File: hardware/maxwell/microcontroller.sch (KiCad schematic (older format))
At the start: 16 parts

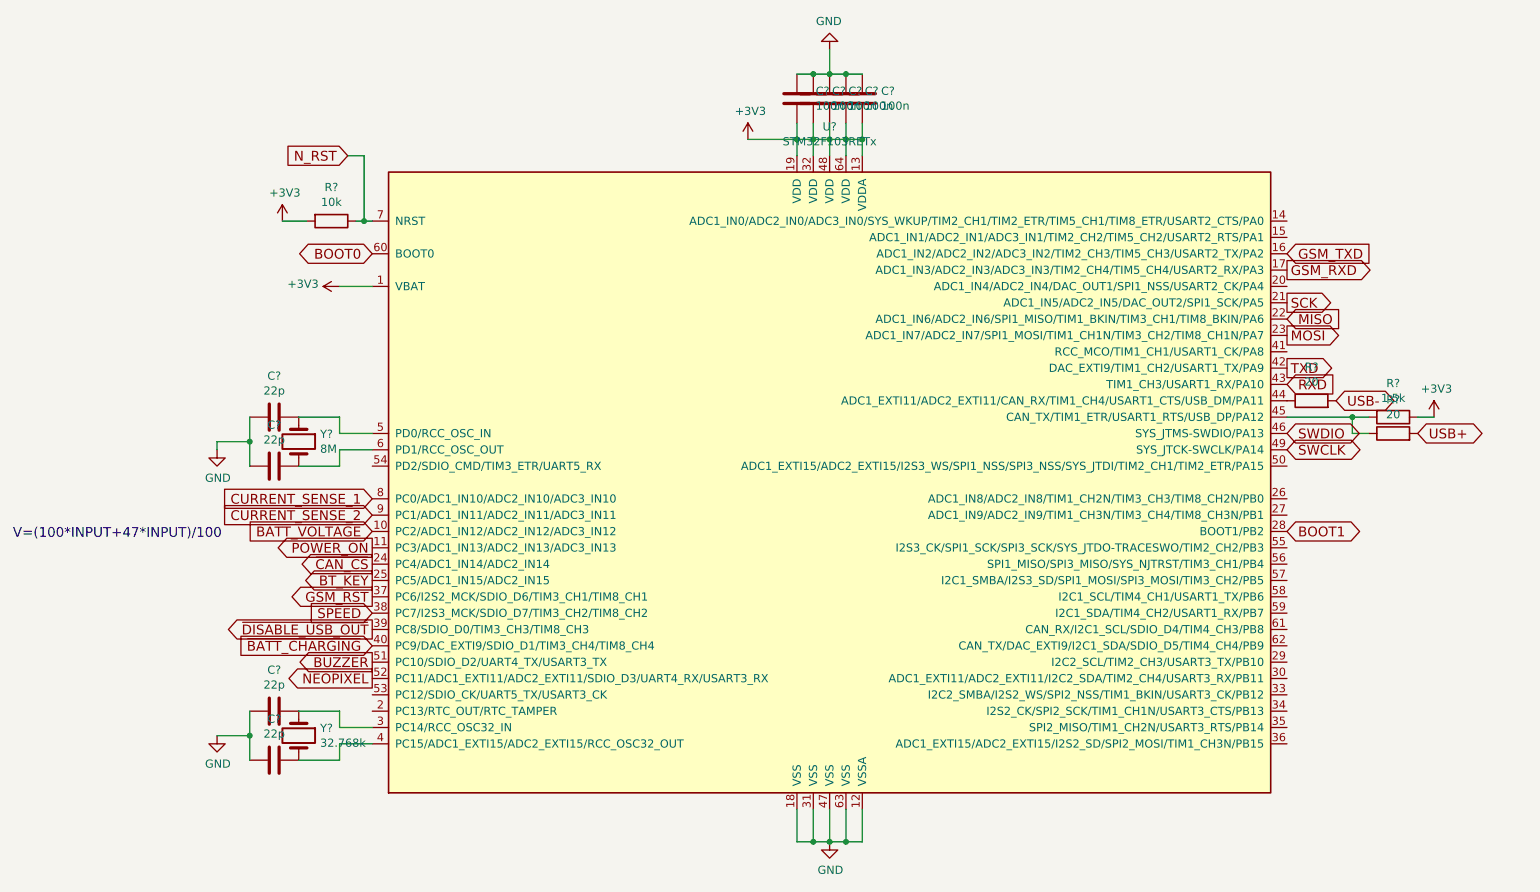
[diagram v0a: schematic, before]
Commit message: Adding finalized PCB layout.
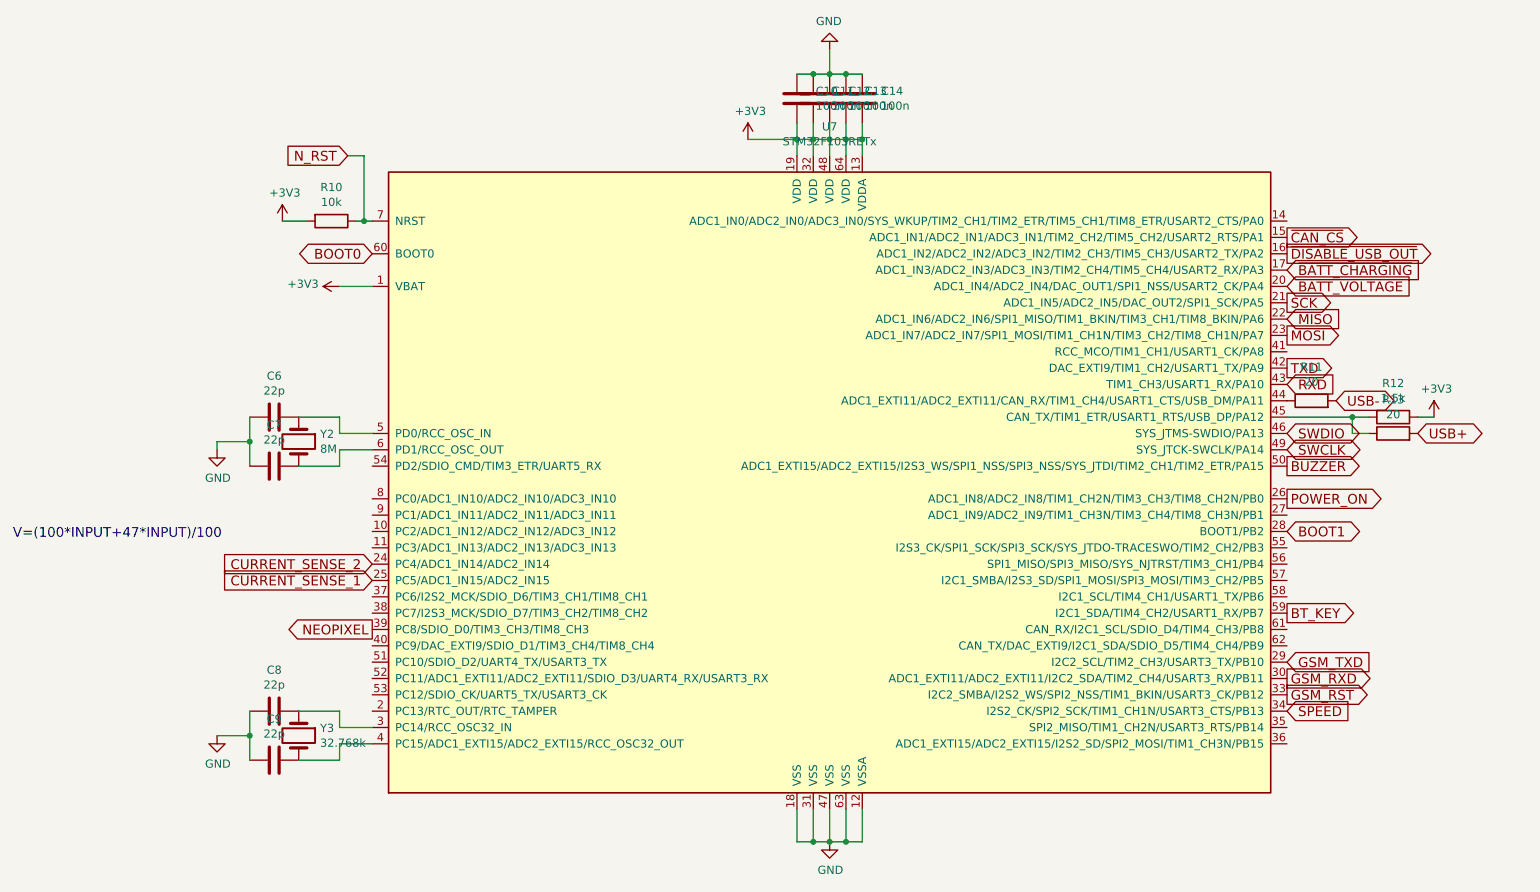
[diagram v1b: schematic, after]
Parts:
- C10, C11, C12, C13, C14, C6, C7, C8, C9: renamed from C?; footprint (none) -> coddingtonbear/coddingtonbear.pretty:0805_Milling
- R10, R11, R12, R13: renamed from R?; footprint (none) -> coddingtonbear/coddingtonbear.pretty:0805_Milling
- U7: renamed from U?; footprint LQFP64 -> kicad-castellated-breakouts:QFP64-1.27MM-CASTELLATED
- Y2: renamed from Y?; footprint (none) -> SchrodingersGat/Components.pretty:crystal_hc-49s
- Y3: renamed from Y?; footprint (none) -> f4grx/f4libs_th.pretty:XTAL32K
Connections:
- net BATT_VOLTAGE: now also U7.20 (ADC1_IN4/ADC2_IN4/DAC_OUT1/SPI1_NSS/USART2_CK/PA4); no longer U7.10 (PC2/ADC1_IN12/ADC2_IN12/ADC3_IN12)
- net BT_KEY: now also U7.59 (I2C1_SDA/TIM4_CH2/USART1_RX/PB7); no longer U7.25 (PC5/ADC1_IN15/ADC2_IN15)
- net BUZZER: now also U7.50 (ADC1_EXTI15/ADC2_EXTI15/I2S3_WS/SPI1_NSS/SPI3_NSS/SYS_JTDI/TIM2_CH1/TIM2_ETR/PA15); no longer U7.51 (PC10/SDIO_D2/UART4_TX/USART3_TX)
- net CURRENT_SENSE_1: now also U7.25 (PC5/ADC1_IN15/ADC2_IN15); no longer U7.8 (PC0/ADC1_IN10/ADC2_IN10/ADC3_IN10)
- net CURRENT_SENSE_2: now also U7.24 (PC4/ADC1_IN14/ADC2_IN14); no longer U7.9 (PC1/ADC1_IN11/ADC2_IN11/ADC3_IN11)
- net GSM_RST: now also U7.33 (I2C2_SMBA/I2S2_WS/SPI2_NSS/TIM1_BKIN/USART3_CK/PB12); no longer U7.37 (PC6/I2S2_MCK/SDIO_D6/TIM3_CH1/TIM8_CH1)
- net GSM_RXD: now also U7.30 (ADC1_EXTI11/ADC2_EXTI11/I2C2_SDA/TIM2_CH4/USART3_RX/PB11); no longer U7.17 (ADC1_IN3/ADC2_IN3/ADC3_IN3/TIM2_CH4/TIM5_CH4/USART2_RX/PA3)
- net GSM_TXD: now also U7.29 (I2C2_SCL/TIM2_CH3/USART3_TX/PB10); no longer U7.16 (ADC1_IN2/ADC2_IN2/ADC3_IN2/TIM2_CH3/TIM5_CH3/USART2_TX/PA2)
- net NEOPIXEL: now also U7.39 (PC8/SDIO_D0/TIM3_CH3/TIM8_CH3); no longer U7.52 (PC11/ADC1_EXTI11/ADC2_EXTI11/SDIO_D3/UART4_RX/USART3_RX)
- net POWER_ON: now also U7.26 (ADC1_IN8/ADC2_IN8/TIM1_CH2N/TIM3_CH3/TIM8_CH2N/PB0); no longer U7.11 (PC3/ADC1_IN13/ADC2_IN13/ADC3_IN13)
- net SPEED: now also U7.34 (I2S2_CK/SPI2_SCK/TIM1_CH1N/USART3_CTS/PB13); no longer U7.38 (PC7/I2S3_MCK/SDIO_D7/TIM3_CH2/TIM8_CH2)
- net ~BATT_CHARGING: now also U7.17 (ADC1_IN3/ADC2_IN3/ADC3_IN3/TIM2_CH4/TIM5_CH4/USART2_RX/PA3); no longer U7.40 (PC9/DAC_EXTI9/SDIO_D1/TIM3_CH4/TIM8_CH4)
- net ~CAN_CS: now also U7.15 (ADC1_IN1/ADC2_IN1/ADC3_IN1/TIM2_CH2/TIM5_CH2/USART2_RTS/PA1); no longer U7.24 (PC4/ADC1_IN14/ADC2_IN14)
- net ~DISABLE_USB_OUT: now also U7.16 (ADC1_IN2/ADC2_IN2/ADC3_IN2/TIM2_CH3/TIM5_CH3/USART2_TX/PA2); no longer U7.39 (PC8/SDIO_D0/TIM3_CH3/TIM8_CH3)
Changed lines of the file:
@@
 $EndDescr
 $Comp
-L STM32F103RETx U?
+L STM32F103RETx U7
 U 1 1 5A1FCF5C
 P 5700 3850
-F 0 "U?" H 5700 6028 50  0000 C CNN
+F 0 "U7" H 5700 6028 50  0000 C CNN
 F 1 "STM32F103RETx" H 5700 5937 50  0000 C CNN
-F 2 "LQFP64" H 8400 5725 50  0001 R TNN
+F 2 "kicad-castellated-breakouts:QFP64-1.27MM-CASTELLATED" H 8400 5725 50  0001 R TNN
 F 3 "" H 5700 3850 50  0001 C CNN
 	1    5700 3850
@@
 $EndComp
 $Comp
-L +3V3 #PWR?
+L +3V3 #PWR022
 U 1 1 5A1FCF63
 P 9400 3450
-F 0 "#PWR?" H 9400 3300 50  0001 C CNN
+F 0 "#PWR022" H 9400 3300 50  0001 C CNN
 F 1 "+3V3" H 9415 3623 50  0000 C CNN
 F 2 "" H 9400 3450 50  0001 C CNN
@@
 $EndComp
 $Comp
-L R R?
+L R R12
 U 1 1 5A1FCF69
 P 9150 3450
-F 0 "R?" V 8943 3450 50  0000 C CNN
+F 0 "R12" V 8943 3450 50  0000 C CNN
 F 1 "1.5k" V 9034 3450 50  0000 C CNN
-F 2 "" V 9080 3450 50  0001 C CNN
+F 2 "coddingtonbear/coddingtonbear.pretty:0805_Milling" V 9080 3450 50  0001 C CNN
 F 3 "" H 9150 3450 50  0001 C CNN
 	1    9150 3450
@@
 USB-
 $Comp
-L R R?
+L R R13
 U 1 1 5A1FCF77
 P 9150 3550
-F 0 "R?" V 9357 3550 50  0000 C CNN
+F 0 "R13" V 9357 3550 50  0000 C CNN
 F 1 "20" V 9266 3550 50  0000 C CNN
-F 2 "" V 9080 3550 50  0001 C CNN
+F 2 "coddingtonbear/coddingtonbear.pretty:0805_Milling" V 9080 3550 50  0001 C CNN
 F 3 "" H 9150 3550 50  0001 C CNN
 	1    9150 3550
@@
 $EndComp
 $Comp
-L R R?
+L R R11
 U 1 1 5A1FCF7E
 P 8650 3350
-F 0 "R?" V 8857 3350 50  0000 C CNN
+F 0 "R11" V 8857 3350 50  0000 C CNN
 F 1 "20" V 8766 3350 50  0000 C CNN
-F 2 "" V 8580 3350 50  0001 C CNN
+F 2 "coddingtonbear/coddingtonbear.pretty:0805_Milling" V 8580 3350 50  0001 C CNN
 F 3 "" H 8650 3350 50  0001 C CNN
 	1    8650 3350
@@
 $EndComp
 $Comp
-L Crystal Y?
+L Crystal Y2
 U 1 1 5A1FCF85
 P 2450 3600
-F 0 "Y?" V 2404 3731 50  0000 L CNN
+F 0 "Y2" V 2404 3731 50  0000 L CNN
 F 1 "8M" V 2495 3731 50  0000 L CNN
-F 2 "" H 2450 3600 50  0001 C CNN
+F 2 "SchrodingersGat/Components.pretty:crystal_hc-49s" H 2450 3600 50  0001 C CNN
 F 3 "" H 2450 3600 50  0001 C CNN
 	1    2450 3600
@@
 $EndComp
 $Comp
-L C C?
+L C C6
 U 1 1 5A1FCF8C
 P 2300 3450
-F 0 "C?" V 2048 3450 50  0000 C CNN
+F 0 "C6" V 2048 3450 50  0000 C CNN
 F 1 "22p" V 2139 3450 50  0000 C CNN
-F 2 "" H 2338 3300 50  0001 C CNN
+F 2 "coddingtonbear/coddingtonbear.pretty:0805_Milling" H 2338 3300 50  0001 C CNN
 F 3 "" H 2300 3450 50  0001 C CNN
 	1    2300 3450
@@
 $EndComp
 $Comp
-L C C?
+L C C7
 U 1 1 5A1FCF93
 P 2300 3750
-F 0 "C?" V 2048 3750 50  0000 C CNN
+F 0 "C7" V 2048 3750 50  0000 C CNN
 F 1 "22p" V 2139 3750 50  0000 C CNN
-F 2 "" H 2338 3600 50  0001 C CNN
+F 2 "coddingtonbear/coddingtonbear.pretty:0805_Milling" H 2338 3600 50  0001 C CNN
 F 3 "" H 2300 3750 50  0001 C CNN
 	1    2300 3750
@@
 $EndComp
 $Comp
-L GND #PWR?
+L GND #PWR023
 U 1 1 5A1FCF9A
 P 1950 3650
-F 0 "#PWR?" H 1950 3400 50  0001 C CNN
+F 0 "#PWR023" H 1950 3400 50  0001 C CNN
 F 1 "GND" H 1955 3477 50  0000 C CNN
 F 2 "" H 1950 3650 50  0001 C CNN
@@
 	2700 3650 2900 3650
 $Comp
-L Crystal Y?
+L Crystal Y3
 U 1 1 5A1FCFAA
 P 2450 5400
-F 0 "Y?" V 2404 5531 50  0000 L CNN
+F 0 "Y3" V 2404 5531 50  0000 L CNN
 F 1 "32.768k" V 2495 5531 50  0000 L CNN
-F 2 "" H 2450 5400 50  0001 C CNN
+F 2 "f4grx/f4libs_th.pretty:XTAL32K" H 2450 5400 50  0001 C CNN
 F 3 "" H 2450 5400 50  0001 C CNN
 	1    2450 5400
@@
 $EndComp
 $Comp
-L C C?
+L C C8
 U 1 1 5A1FCFB1
 P 2300 5250
-F 0 "C?" V 2048 5250 50  0000 C CNN
+F 0 "C8" V 2048 5250 50  0000 C CNN
 F 1 "22p" V 2139 5250 50  0000 C CNN
-F 2 "" H 2338 5100 50  0001 C CNN
+F 2 "coddingtonbear/coddingtonbear.pretty:0805_Milling" H 2338 5100 50  0001 C CNN
 F 3 "" H 2300 5250 50  0001 C CNN
 	1    2300 5250
@@
 $EndComp
 $Comp
-L C C?
+L C C9
 U 1 1 5A1FCFB8
 P 2300 5550
-F 0 "C?" V 2048 5550 50  0000 C CNN
+F 0 "C9" V 2048 5550 50  0000 C CNN
 F 1 "22p" V 2139 5550 50  0000 C CNN
-F 2 "" H 2338 5400 50  0001 C CNN
+F 2 "coddingtonbear/coddingtonbear.pretty:0805_Milling" H 2338 5400 50  0001 C CNN
 F 3 "" H 2300 5550 50  0001 C CNN
 	1    2300 5550
@@
 $EndComp
 $Comp
-L GND #PWR?
+L GND #PWR024
 U 1 1 5A1FCFBF
 P 1950 5400
-F 0 "#PWR?" H 1950 5150 50  0001 C CNN
+F 0 "#PWR024" H 1950 5150 50  0001 C CNN
 F 1 "GND" H 1955 5227 50  0000 C CNN
 F 2 "" H 1950 5400 50  0001 C CNN
@@
 Connection ~ 2150 5400
 $Comp
-L GND #PWR?
+L GND #PWR025
 U 1 1 5A1FCFCE
 P 5700 6050
-F 0 "#PWR?" H 5700 5800 50  0001 C CNN
+F 0 "#PWR025" H 5700 5800 50  0001 C CNN
 F 1 "GND" H 5705 5877 50  0000 C CNN
 F 2 "" H 5700 6050 50  0001 C CNN
@@
 BOOT0
 $Comp
-L R R?
+L R R10
 U 1 1 5A1FCFDF
 P 2650 2250
-F 0 "R?" V 2443 2250 50  0000 C CNN
+F 0 "R10" V 2443 2250 50  0000 C CNN
 F 1 "10k" V 2534 2250 50  0000 C CNN
-F 2 "" V 2580 2250 50  0001 C CNN
+F 2 "coddingtonbear/coddingtonbear.pretty:0805_Milling" V 2580 2250 50  0001 C CNN
 F 3 "" H 2650 2250 50  0001 C CNN
 	1    2650 2250
@@
 $EndComp
 $Comp
-L +3V3 #PWR?
+L +3V3 #PWR026
 U 1 1 5A1FCFE6
 P 2350 2250
-F 0 "#PWR?" H 2350 2100 50  0001 C CNN
+F 0 "#PWR026" H 2350 2100 50  0001 C CNN
 F 1 "+3V3" H 2365 2423 50  0000 C CNN
 F 2 "" H 2350 2250 50  0001 C CNN
@@
 	2500 2250 2350 2250
 $Comp
-L C C?
+L C C10
 U 1 1 5A1FCFEE
 P 5500 1500
-F 0 "C?" H 5385 1454 50  0000 R CNN
+F 0 "C10" H 5385 1454 50  0000 R CNN
 F 1 "100n" H 5385 1545 50  0000 R CNN
-F 2 "" H 5538 1350 50  0001 C CNN
+F 2 "coddingtonbear/coddingtonbear.pretty:0805_Milling" H 5538 1350 50  0001 C CNN
 F 3 "" H 5500 1500 50  0001 C CNN
 	1    5500 1500
@@
 $EndComp
 $Comp
-L C C?
+L C C11
 U 1 1 5A1FCFF5
 P 5600 1500
-F 0 "C?" H 5485 1454 50  0000 R CNN
+F 0 "C11" H 5485 1454 50  0000 R CNN
 F 1 "100n" H 5485 1545 50  0000 R CNN
-F 2 "" H 5638 1350 50  0001 C CNN
+F 2 "coddingtonbear/coddingtonbear.pretty:0805_Milling" H 5638 1350 50  0001 C CNN
 F 3 "" H 5600 1500 50  0001 C CNN
 	1    5600 1500
@@
 $EndComp
 $Comp
-L C C?
+L C C12
 U 1 1 5A1FCFFC
 P 5700 1500
-F 0 "C?" H 5585 1454 50  0000 R CNN
+F 0 "C12" H 5585 1454 50  0000 R CNN
 F 1 "100n" H 5585 1545 50  0000 R CNN
-F 2 "" H 5738 1350 50  0001 C CNN
+F 2 "coddingtonbear/coddingtonbear.pretty:0805_Milling" H 5738 1350 50  0001 C CNN
 F 3 "" H 5700 1500 50  0001 C CNN
 	1    5700 1500
@@
 $EndComp
 $Comp
-L C C?
+L C C13
 U 1 1 5A1FD003
 P 5800 1500
-F 0 "C?" H 5685 1454 50  0000 R CNN
+F 0 "C13" H 5685 1454 50  0000 R CNN
 F 1 "100n" H 5685 1545 50  0000 R CNN
-F 2 "" H 5838 1350 50  0001 C CNN
+F 2 "coddingtonbear/coddingtonbear.pretty:0805_Milling" H 5838 1350 50  0001 C CNN
 F 3 "" H 5800 1500 50  0001 C CNN
 	1    5800 1500
@@
 $EndComp
 $Comp
-L C C?
+L C C14
 U 1 1 5A1FD00A
 P 5900 1500
-F 0 "C?" H 5785 1454 50  0000 R CNN
+F 0 "C14" H 5785 1454 50  0000 R CNN
 F 1 "100n" H 5785 1545 50  0000 R CNN
-F 2 "" H 5938 1350 50  0001 C CNN
+F 2 "coddingtonbear/coddingtonbear.pretty:0805_Milling" H 5938 1350 50  0001 C CNN
 F 3 "" H 5900 1500 50  0001 C CNN
 	1    5900 1500
@@
 $EndComp
 $Comp
-L GND #PWR?
+L GND #PWR027
 U 1 1 5A1FD011
 P 5700 1200
-F 0 "#PWR?" H 5700 950 50  0001 C CNN
+F 0 "#PWR027" H 5700 950 50  0001 C CNN
 F 1 "GND" H 5705 1027 50  0000 C CNN
 F 2 "" H 5700 1200 50  0001 C CNN
@@
 $EndComp
 $Comp
-L +3V3 #PWR?
+L +3V3 #PWR028
 U 1 1 5A1FD017
 P 5200 1750
-F 0 "#PWR?" H 5200 1600 50  0001 C CNN
+F 0 "#PWR028" H 5200 1600 50  0001 C CNN
 F 1 "+3V3" H 5215 1923 50  0000 C CNN
 F 2 "" H 5200 1750 50  0001 C CNN
@@
 	5700 1200 5700 1350
 $Comp
-L +3V3 #PWR?
+L +3V3 #PWR029
 U 1 1 5A1FD02D
 P 2700 2650
-F 0 "#PWR?" H 2700 2500 50  0001 C CNN
+F 0 "#PWR029" H 2700 2500 50  0001 C CNN
 F 1 "+3V3" V 2715 2778 50  0000 L CNN
 F 2 "" H 2700 2650 50  0001 C CNN
@@
 Text GLabel 8500 3650 2    60   BiDi ~ 0
 SWCLK
-Text GLabel 2900 4650 0    60   Input ~ 0
+Text GLabel 8500 5250 2    60   Input ~ 0
 SPEED
-Text GLabel 2900 4750 0    60   Output ~ 0
+Text GLabel 8500 2450 2    60   Output ~ 0
 ~DISABLE_USB_OUT
-Text GLabel 2900 4850 0    60   Input ~ 0
+Text GLabel 8500 2550 2    60   Input ~ 0
 ~BATT_CHARGING
-Text GLabel 2900 4250 0    60   Output ~ 0
+Text GLabel 8500 3950 2    60   Output ~ 0
 POWER_ON
 Text GLabel 8500 2750 2    60   Output ~ 0
@@
 Text GLabel 8500 2950 2    60   Output ~ 0
 MOSI
-Text GLabel 2900 4350 0    60   Output ~ 0
+Text GLabel 8500 2350 2    60   Output ~ 0
 ~CAN_CS
 Text GLabel 8500 3150 2    60   Output ~ 0
@@
 Text GLabel 8500 3250 2    60   Input ~ 0
 RXD
-Text GLabel 2900 4450 0    60   Output ~ 0
+Text GLabel 8500 4650 2    60   Output ~ 0
 BT_KEY
-Text GLabel 8500 2450 2    60   Input ~ 0
+Text GLabel 8500 4950 2    60   Input ~ 0
 GSM_TXD
-Text GLabel 8500 2550 2    60   Output ~ 0
+Text GLabel 8500 5050 2    60   Output ~ 0
 GSM_RXD
-Text GLabel 2900 4550 0    60   Output ~ 0
+Text GLabel 8500 5150 2    60   Output ~ 0
 GSM_RST
-Text GLabel 2900 3950 0    60   Input ~ 0
+Text GLabel 2900 4450 0    60   Input ~ 0
 CURRENT_SENSE_1
-Text GLabel 2900 4050 0    60   Input ~ 0
+Text GLabel 2900 4350 0    60   Input ~ 0
 CURRENT_SENSE_2
-Text GLabel 2900 4150 0    60   Input ~ 0
+Text GLabel 8500 2650 2    60   Input ~ 0
 BATT_VOLTAGE
 Text Notes 700  4200 0    60   ~ 0
 V=(100*INPUT+47*INPUT)/100
-Text GLabel 2900 4950 0    60   Output ~ 0
+Text GLabel 8500 3750 2    60   Output ~ 0
 BUZZER
-Text GLabel 2900 5050 0    60   Output ~ 0
+Text GLabel 2900 4750 0    60   Output ~ 0
 NEOPIXEL
 Text GLabel 2750 1850 0    60   Input ~ 0

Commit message: Updating schematic to add reverse polarity protection, higher-current diodes for zener limiting, and a low-side n-channel mosfet for enabling/disabling devices receiving direct battery power (limiting that quiescent current as much as possible).
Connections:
- net ENABLE_BATT_POWER: now reaches U7.62 (CAN_TX/DAC_EXTI9/I2C1_SDA/SDIO_D5/TIM4_CH4/PB9)
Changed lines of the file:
@@
 	2850 1850 2850 2250
 Connection ~ 2850 2250
+Text GLabel 8500 4850 2    60   Output ~ 0
+ENABLE_BATT_POWER
 $EndSCHEMATC

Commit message: More minor changes and fixes.
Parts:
- added R26: 1k, coddingtonbear/coddingtonbear.pretty:0805_Milling, symbol R
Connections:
- net POWER_ON: now also R26.1; no longer U7.26 (ADC1_IN8/ADC2_IN8/TIM1_CH2N/TIM3_CH3/TIM8_CH2N/PB0)
- net USB_PRER-: now reaches R11.1, U7.44 (ADC1_EXTI11/ADC2_EXTI11/CAN_RX/TIM1_CH4/USART1_CTS/USB_DM/PA11)
- net USB_PRER+: now reaches R12.2, R13.1, U7.45 (CAN_TX/TIM1_ETR/USART1_RTS/USB_DP/PA12)
- net ~DISABLE_USB_OUT renamed ENABLE_USB_OUT
- new net: R26.2, U7.26 (ADC1_IN8/ADC2_IN8/TIM1_CH2N/TIM3_CH3/TIM8_CH2N/PB0)
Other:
- moved on the sheet: R11
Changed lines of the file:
@@
 	8900 3550 8900 3450
 Connection ~ 8900 3450
-Text GLabel 8800 3350 2    60   BiDi ~ 0
+Text GLabel 9550 3350 2    60   BiDi ~ 0
 USB-
 $Comp
@@
 L R R11
 U 1 1 5A1FCF7E
-P 8650 3350
-F 0 "R11" V 8857 3350 50  0000 C CNN
-F 1 "20" V 8766 3350 50  0000 C CNN
-F 2 "coddingtonbear/coddingtonbear.pretty:0805_Milling" V 8580 3350 50  0001 C CNN
-F 3 "" H 8650 3350 50  0001 C CNN
-	1    8650 3350
+P 9400 3350
+F 0 "R11" V 9607 3350 50  0000 C CNN
+F 1 "20" V 9516 3350 50  0000 C CNN
+F 2 "coddingtonbear/coddingtonbear.pretty:0805_Milling" V 9330 3350 50  0001 C CNN
+F 3 "" H 9400 3350 50  0001 C CNN
+	1    9400 3350
 	0    -1   -1   0
 $EndComp
@@
 SPEED
 Text GLabel 8500 2450 2    60   Output ~ 0
-~DISABLE_USB_OUT
+ENABLE_USB_OUT
 Text GLabel 8500 2550 2    60   Input ~ 0
 ~BATT_CHARGING
-Text GLabel 8500 3950 2    60   Output ~ 0
+Text GLabel 8800 3950 2    60   Output ~ 0
 POWER_ON
 Text GLabel 8500 2750 2    60   Output ~ 0
@@
 Text GLabel 8500 4850 2    60   Output ~ 0
 ENABLE_BATT_POWER
+$Comp
+L R R26
+U 1 1 5A260AAF
+P 8650 3950
+F 0 "R26" V 8443 3950 50  0000 C CNN
+F 1 "1k" V 8534 3950 50  0000 C CNN
+F 2 "coddingtonbear/coddingtonbear.pretty:0805_Milling" V 8580 3950 50  0001 C CNN
+F 3 "" H 8650 3950 50  0001 C CNN
+	1    8650 3950
+	0    1    1    0
+$EndComp
+Wire Wire Line
+	8500 3350 9250 3350
+Text Label 8600 3350 0    60   ~ 0
+USB_PRER-
+Text Label 8600 3450 0    60   ~ 0
+USB_PRER+
 $EndSCHEMATC

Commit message: More fixes, additions, improvements.
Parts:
- added R33: 1M, coddingtonbear/coddingtonbear.pretty:0805_Milling, symbol R
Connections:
- net CAN_INT: now reaches U7.14 (ADC1_IN0/ADC2_IN0/ADC3_IN0/SYS_WKUP/TIM2_CH1/TIM2_ETR/TIM5_CH1/TIM8_ETR/USART2_CTS/PA0)
- net DYNAMO_VOLTAGE: now reaches U7.27 (ADC1_IN9/ADC2_IN9/TIM1_CH3N/TIM3_CH4/TIM8_CH3N/PB1)
- net BATT_CHARGE_ENABLE: now reaches U7.35 (SPI2_MISO/TIM1_CH2N/USART3_RTS/PB14)
- net at C6.1, U7.5 (PD0/RCC_OSC_IN), Y2.1: now also R33.2
- net at C7.1, U7.6 (PD1/RCC_OSC_OUT), Y2.2: now also R33.1
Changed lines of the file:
@@
 	1950 3600 2150 3600
 Connection ~ 2150 3600
-Wire Wire Line
-	2450 3450 2700 3450
-Wire Wire Line
-	2700 3450 2700 3550
-Wire Wire Line
-	2700 3550 2900 3550
-Wire Wire Line
-	2450 3750 2700 3750
-Wire Wire Line
-	2700 3750 2700 3650
-Wire Wire Line
-	2700 3650 2900 3650
 $Comp
 L Crystal Y3
@@
 	1    0    0    -1
 $EndComp
-Wire Wire Line
-	2450 5250 2700 5250
-Wire Wire Line
-	2700 5250 2700 5350
-Wire Wire Line
-	2700 5350 2900 5350
-Wire Wire Line
-	2450 5550 2700 5550
-Wire Wire Line
-	2700 5550 2700 5450
-Wire Wire Line
-	2700 5450 2900 5450
 Wire Wire Line
 	2150 5250 2150 5550
@@
 Text Label 8600 3450 0    60   ~ 0
 USB_PRER+
+Text GLabel 8500 2250 2    60   Input ~ 0
+CAN_INT
+$Comp
+L R R33
+U 1 1 5A2732F7
+P 2700 3600
+F 0 "R33" V 2493 3600 50  0000 C CNN
+F 1 "1M" V 2584 3600 50  0000 C CNN
+F 2 "coddingtonbear/coddingtonbear.pretty:0805_Milling" V 2630 3600 50  0001 C CNN
+F 3 "" H 2700 3600 50  0001 C CNN
+	1    2700 3600
+	-1   0    0    1
+$EndComp
+Wire Wire Line
+	2450 5250 2800 5250
+Wire Wire Line
+	2800 5250 2800 5350
+Wire Wire Line
+	2800 5350 2900 5350
+Wire Wire Line
+	2900 5450 2800 5450
+Wire Wire Line
+	2800 5450 2800 5550
+Wire Wire Line
+	2800 5550 2450 5550
+Wire Wire Line
+	2450 3450 2800 3450
+Wire Wire Line
+	2800 3450 2800 3550
+Wire Wire Line
+	2800 3550 2900 3550
+Connection ~ 2700 3450
+Wire Wire Line
+	2450 3750 2800 3750
+Wire Wire Line
+	2800 3750 2800 3650
+Wire Wire Line
+	2800 3650 2900 3650
+Connection ~ 2700 3750
+Text GLabel 8500 4050 2    60   Input ~ 0
+DYNAMO_VOLTAGE
+Text GLabel 8500 5350 2    60   Output ~ 0
+BATT_CHARGE_ENABLE
 $EndSCHEMATC

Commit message: Fixed just...an unbelievable number of bugs.
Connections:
- net BUZZER: now also U7.58 (I2C1_SCL/TIM4_CH1/USART1_TX/PB6); no longer U7.50 (ADC1_EXTI15/ADC2_EXTI15/I2S3_WS/SPI1_NSS/SPI3_NSS/SYS_JTDI/TIM2_CH1/TIM2_ETR/PA15)
- net BATT_CHARGE_ENABLE renamed ~BATT_CHARGE_ENABLE
- net ENABLE_USB_OUT renamed ~ENABLE_USB_OUT
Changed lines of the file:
@@
 SPEED
 Text GLabel 8500 2450 2    60   Output ~ 0
-ENABLE_USB_OUT
+~ENABLE_USB_OUT
 Text GLabel 8500 2550 2    60   Input ~ 0
 ~BATT_CHARGING
@@
 Text Notes 700  4200 0    60   ~ 0
 V=(100*INPUT+47*INPUT)/100
-Text GLabel 8500 3750 2    60   Output ~ 0
+Text GLabel 8500 4550 2    60   Output ~ 0
 BUZZER
 Text GLabel 2900 4750 0    60   Output ~ 0
@@
 DYNAMO_VOLTAGE
 Text GLabel 8500 5350 2    60   Output ~ 0
-BATT_CHARGE_ENABLE
+~BATT_CHARGE_ENABLE
 $EndSCHEMATC
